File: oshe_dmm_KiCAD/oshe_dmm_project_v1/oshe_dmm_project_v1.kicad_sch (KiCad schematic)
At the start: 70 parts, among them J1 FTDI Basic, J2 USB_C_Receptacle_PowerOnly_6P, J3 ON/OFF, SW1 SW_Push, SW2 SW_Rotary_1x4_MP, U1 ATmega328P-A, U2 INA219BxD, U3 BQ24075RGT, U4 LM317_SOT-223, U5 MCP6001-OT, U6 ADS1115IDGS, Y1 16MHz

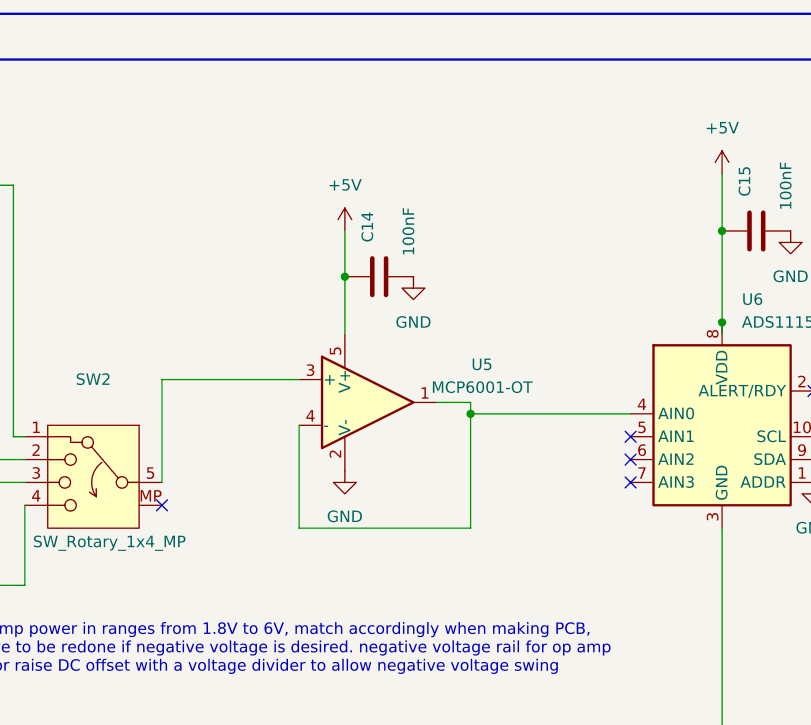
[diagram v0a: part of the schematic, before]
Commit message: updated voltage circuit.
Allows negative voltage measurement
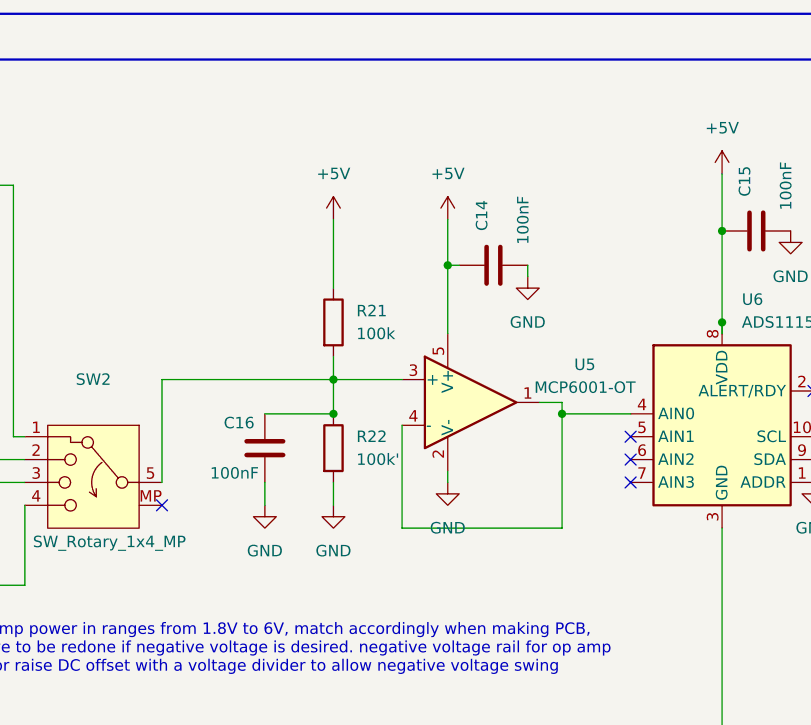
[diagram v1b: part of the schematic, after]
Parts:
- added C16: 100nF, symbol Device:C
- added R21: 100k, symbol Device:R
- added R22: 100k', symbol Device:R
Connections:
- net +5V: now also R21.1
- net GND: now also C16.2, R22.2
- net at SW2.5, U5.3 (+): now also C16.1, R21.2, R22.1
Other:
- moved on the sheet: C14, U5

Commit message: ,,k
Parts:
- added R1: 220K, Resistor_SMD:R_1206_3216Metric, symbol Device:R_US
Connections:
- net +5V: now also R1.1; no longer DS1.15 (LED(+))
- new net: DS1.15 (LED(+)), R1.2
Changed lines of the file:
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@@
 	(wire
 		(pts
+			(xy 190.5 44.45) (xy 193.04 44.45)
+		)
+		(stroke
+			(width 0)
+			(type default)
+		)
+	)
+	(wire
+		(pts
 			(xy 236.22 73.66) (xy 236.22 74.93)
 		)
@@
 	(wire
 		(pts
-			(xy 176.53 36.83) (xy 180.34 36.83)
+			(xy 176.53 36.83) (xy 190.5 36.83)
 		)
 		(stroke
@@
 	(label "R-ILIM"
 		(at 294.64 69.85 0)
-		(fields_autoplaced yes)
 		(effects
 			(font
@@
 	(label "200v"
 		(at 265.43 187.96 0)
-		(fields_autoplaced yes)
 		(effects
 			(font
@@
 	(label "200mv"
 		(at 265.43 143.51 0)
-		(fields_autoplaced yes)
 		(effects
 			(font
@@
 	(label "20v"
 		(at 262.89 176.53 0)
-		(fields_autoplaced yes)
 		(effects
 			(font
@@
 	(label "R-ISET"
 		(at 303.53 69.85 0)
-		(fields_autoplaced yes)
 		(effects
 			(font
@@
 	(label "2v"
 		(at 264.16 158.75 0)
-		(fields_autoplaced yes)
 		(effects
 			(font
@@
 	(global_label "+5V"
 		(shape input)
-		(at 180.34 36.83 0)
+		(at 193.04 44.45 0)
 		(fields_autoplaced yes)
 		(effects
@@
 		)
 		(property "Intersheetrefs" "${INTERSHEET_REFS}"
-			(at 187.1957 36.83 0)
+			(at 199.8957 44.45 0)
 			(effects
 				(font
@@
 					(unit 1)
 				)
+			)
+		)
+	)
+	(symbol
+		(lib_name "R_US_1")
+		(lib_id "Device:R_US")
+		(at 190.5 40.64 180)
+		(unit 1)
+		(exclude_from_sim no)
+		(in_bom yes)
+		(on_board yes)
+		(dnp no)
+		(fields_autoplaced yes)
+		(property "Reference" "R1"
+			(at 193.04 39.3699 0)
+			(effects
+				(font
+					(size 1.27 1.27)
+				)
+				(justify right)
+			)
+		)
+		(property "Value" "220K"
+			(at 193.04 41.9099 0)
+			(effects
+				(font
+					(size 1.27 1.27)
+				)
+				(justify right)
+			)
+		)
+		(property "Footprint" "Resistor_SMD:R_1206_3216Metric"
+			(at 189.484 40.386 90)
+			(effects
+				(font
+					(size 1.27 1.27)
+				)
+				(hide yes)
+			)
+		)
+		(property "Datasheet" "~"
+			(at 190.5 40.64 0)
+			(effects
+				(font
+					(size 1.27 1.27)
+				)
+				(hide yes)
+			)
+		)
+		(property "Description" "Resistor, US symbol"
+			(at 190.5 40.64 0)
+			(effects
+				(font
+					(size 1.27 1.27)
+				)
+				(hide yes)
+			)
+		)
+		(pin "1"
+		)
+		(pin "2"
+		)
+		(instances
+			(project ""
+				(path "/24c8480a-c336-4df0-8536-7016ee8fc0ac"
+					(reference "R1")
+					(unit 1)
+				)

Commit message: More changes plus custom footprints and symbols!
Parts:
- removed SW1: SW_Push, Button_Switch_SMD:SW_Push_1P1T-MP_NO_Horizontal_Alps_SKRTLAE010, symbol Switch:SW_Push
- added F1: 5A, Fuse:Fuseholder_Clip-5x20mm_Keystone_3512P_Inline_P23.62x7.27mm_D1.02x2.41x1.02x1.57mm_Horizontal, symbol Device:Fuse
- added SW1: PTS526 SK15 SMTR2 LFS, DMM_Footprint_Library:SMT_FS, symbol DMM_Symbol_Library:PTS526_SK15_SMTR2_LFS
- F2: renamed from F1; value Fuse -> 500mA
- renumbered C16 to C10, C14 to C11, C10 to C12, C11 to C13, C15 to C14, C12 to C15, C13 to C16, R2 to R1, R15 to R10, R16 to R11, R17 to R12, R18 to R13, R9 to R14, R10 to R15, R11 to R16, R21 to R17, R22 to R18, R12 to R19, R1 to R2, R14 to R20, R13 to R21, R19 to R22, R20 to R23, R4 to R3, R3 to R4, R1 to R8, R8 to R9, RV2 to RV1, RV1 to RV2, U5 to U4, U4 to U5
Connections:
- net Current Positive: now also F1.1; no longer R1.1, U2.8 (IN+)
- net GND: now also SW1.3, SW1.4
- net at C5.1, R7.1, U1.29 (~{RESET}/PC6): now also SW1.1, SW1.2
- new net: F1.2, R1.1, U2.8 (IN+)
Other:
- note added: "Switching System"
- note added: "Voltage Input Protection"
- note removed: "Input Protection"
- moved on the sheet: C2, C4, COMin1, D1, DS1, F2, R1, R2, R3, R4, R5, R8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

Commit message: Friday Library Meeting
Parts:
- removed C10, C11: 100nF, symbol Device:C
- removed C4: 0.15 μf, oshe:CKG57K, symbol Device:C
- removed COMin1, Vin1: ~, symbol oshe:Input
- removed D1: SMAJ200CA, Diode_SMD:D_SMA, symbol Diode:SMAJ200CA
- removed R12: 9k, symbol Device:R
- removed R17: 100k, symbol Device:R
- removed R18: 100k', symbol Device:R
- removed RV2: Varistor, symbol Device:Varistor
- removed SW2: SW_Rotary_1x4_MP, symbol Switch:SW_Rotary_1x4_MP
- removed TP1: V-, symbol Connector:TestPoint_Probe
- removed TP2: V+, symbol Connector:TestPoint_Probe
- removed U4: MCP6001-OT, Package_TO_SOT_SMD:SOT-23-5, symbol Amplifier_Operational:MCP6001-OT
- removed Vout+1, Vout-1: ~, symbol oshe:Node
- added D5: D_TVS, symbol Device:D_TVS
- added D6: SMAJ200CA, Diode_SMD:D_SMA, symbol Diode:SMAJ200CA
- added J4: Voltage, CONN_575-8_KEY, symbol DMM_Symbol_Library:575-8
- added J5: GND, CONN_575-8_KEY, symbol DMM_Symbol_Library:575-8
- added J6: Current, CONN_575-8_KEY, symbol DMM_Symbol_Library:575-8
- added R12: 1k, Resistor_SMD:R_1206_3216Metric_Pad1.30x1.75mm_HandSolder, symbol Device:R_US
- C14: footprint (none) -> Capacitor_SMD:C_1206_3216Metric_Pad1.33x1.80mm_HandSolder
- R10, R11, R22, R23: footprint (none) -> Resistor_SMD:R_1206_3216Metric_Pad1.30x1.75mm_HandSolder
- R13: value 1k -> 10k; footprint (none) -> Resistor_SMD:R_1206_3216Metric_Pad1.30x1.75mm_HandSolder
- R2: value R_US -> 1k
- R3: value 10k -> 1k
- R8: footprint Resistor_SMD:R_1206_3216Metric -> Resistor_SMD:R_1206_3216Metric_Pad1.30x1.75mm_HandSolder
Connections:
- net 200mv is gone; now on net 2V_Rang: R10.1
- net 20v is gone; now on net 200V_Rang: R11.2
- net Current Negative is gone; now on net Input_Negative: R1.2, U2.7 (IN-)
- net A0: now also R2.1, R3.1, R12.1
- net GND: no longer R13.2
- net Voltage_Input: now reaches F2.1
- net Voltage_Input: now also J4.1
- net 2V_Rang: now reaches F2.2
- net 2V_Rang: now also D6.2 (A2); no longer R2.1
- net at R2.2: no longer R3.1
- net V_ADC_Input: now reaches U6.4 (AIN0)
- net V_ADC_Input: now also D5.2 (A2)
- net Input_Negative: now reaches U6.5 (AIN1)
- net Input_Negative: now also R13.2, D5.1 (A1), D6.1 (A1), J5.1
- net 200v renamed 200V_Rang
- net 2v renamed 20V_Rang
- net Current Positive renamed Current_Input
- net Current_Input: now also J6.1
- no-connect marks 12 -> 10
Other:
- note added: "Finish switching mechanism (modes going to right spot, range indications) pick out components (custom footprints?) finalize BoM"
- note removed: "Op amp power in ranges from 1.8V to 6V, match accordingly when making PCB, will have to be redone if negative voltage is desired. negative voltage rail for op amp or raise DC offset with a voltage divider to allow negative voltage swing"
- note removed: "Voltage Input Protection"
- moved on the sheet: C14, F1, R10, R11, R13, R22, R23, U6

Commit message: Made some updates
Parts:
- removed C14: 100nF, Capacitor_SMD:C_1206_3216Metric_Pad1.33x1.80mm_HandSolder, symbol Device:C
- added C11: 0.1uF, Capacitor_SMD:C_1206_3216Metric_Pad1.33x1.80mm_HandSolder, symbol Device:C
- added J10, J9: Voltage Range 2, Connector_PinHeader_2.54mm:PinHeader_1x02_P2.54mm_Vertical, symbol Connector_Generic:Conn_01x02
- added J11, J12: Voltage Range 3, Connector_PinHeader_2.54mm:PinHeader_1x02_P2.54mm_Vertical, symbol Connector_Generic:Conn_01x02
- added J13: Current, Connector_PinHeader_2.54mm:PinHeader_1x02_P2.54mm_Vertical, symbol Connector_Generic:Conn_01x02
- added J14, J15: Resistance, Connector_PinHeader_2.54mm:PinHeader_1x02_P2.54mm_Vertical, symbol Connector_Generic:Conn_01x02
- added J7, J8: Voltage Range 1, Connector_PinHeader_2.54mm:PinHeader_1x02_P2.54mm_Vertical, symbol Connector_Generic:Conn_01x02
- added R10, R9: 1k, Resistor_SMD:R_1206_3216Metric_Pad1.30x1.75mm_HandSolder, symbol Device:R_US
- J2: renamed from J4; footprint CONN_575-8_KEY -> DMM_Footprint_Library:CONN_575-8_KEY
- J3: renamed from J5; footprint CONN_575-8_KEY -> DMM_Footprint_Library:CONN_575-8_KEY
- J4: renamed from J6; footprint CONN_575-8_KEY -> DMM_Footprint_Library:CONN_575-8_KEY
- R14: renamed from R10; symbol Device:R -> Device:R_US
- R15: renamed from R11; symbol Device:R -> Device:R_US
- R16: renamed from R13; symbol Device:R -> Device:R_US
- R22, R23: symbol Device:R -> Device:R_US
- renumbered C13 to C10, C15 to C12, C16 to C13, C3 to C2, C2 to C3, C5 to C4, C6 to C5, C7 to C6, C8 to C7, C9 to C8, C12 to C9, D2 to D1, D6 to D2, D5 to D3, D3 to D4, D4 to D5, J2 to J5, J3 to J6, R8 to R11, R9 to R12, R14 to R13, R15 to R17, R16 to R18, R4 to R2, R2 to R3, R3 to R4, R12 to R5, R5 to R7, R7 to R8, U5 to U4, U6 to U5
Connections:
- net +5V: now also C11.2, J10.1 (Pin_1), J12.1 (Pin_1), J13.1 (Pin_1), J15.1 (Pin_1), J8.1 (Pin_1)
- net 200V_Rang: now also J11.1 (Pin_1)
- net 20V_Rang: now also J9.1 (Pin_1)
- net 2V_Rang: now also D2.1 (A1), J7.1 (Pin_1); no longer D2.2 (A2)
- net A0: no longer R3.1, R4.1, R5.1
- net A3: now also R3.1, R4.1, R5.1, R10.1, R9.1
- net GND: now also C11.1
- net Input_Negative: now also D2.2 (A2); no longer D2.1 (A1)
- net V_ADC_Input: now also J11.2 (Pin_2), J7.2 (Pin_2), J9.2 (Pin_2)
- net Voltage_Input: now also J14.1 (Pin_1)
- net at R4.2: now also J10.2 (Pin_2)
- net at R5.2: now also J12.2 (Pin_2)
- net at R3.2: now also J8.2 (Pin_2)
- new net: J13.2 (Pin_2), R9.2
- new net: J15.2 (Pin_2), R10.2
- new net R_ADC_Input: J14.2 (Pin_2)
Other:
- note added: "Input Jacks"
- moved on the sheet: D2, D3, F2, J2, J3, J4, R2, R3, R4, R5, R7, U5

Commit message: Trying to fit everything on the board
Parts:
- D2: renamed from D3; footprint (none) -> Diode_SMD:D_0805_2012Metric_Pad1.15x1.40mm_HandSolder
- F1: renamed from F2; footprint Fuse:Fuseholder_Clip-5x20mm_Keystone_3512P_Inline_P23.62x7.27mm_D1.02x2.41x1.02x1.57mm_Horizontal -> DMM_Footprint_Library:FUSE_4628
- F2: renamed from F1; footprint Fuse:Fuseholder_Clip-5x20mm_Keystone_3512P_Inline_P23.62x7.27mm_D1.02x2.41x1.02x1.57mm_Horizontal -> DMM_Footprint_Library:FUSE_4628
- renumbered C9 to C10, C10 to C11, C11 to C7, C7 to C8, C8 to C9, D2 to D1, D1 to D3, R23 to R10, R17 to R14, R18 to R15, R3 to R16, R4 to R17, R5 to R18, R14 to R2, R9 to R22, R10 to R23, R15 to R3, R16 to R4, R2 to R5, R7 to R6, R6 to R7, R22 to R9, U5 to U3, U3 to U4, U4 to U5
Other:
- moved on the sheet: C7, D1, D2, F1, J10, J11, J12, J13, J14, J15, J7, J8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

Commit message: PCB is almost done!
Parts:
- removed J14, J15: Resistance, Connector_PinHeader_2.54mm:PinHeader_1x02_P2.54mm_Vertical, symbol Connector_Generic:Conn_01x02
- removed R23: 1k, Resistor_SMD:R_1206_3216Metric_Pad1.30x1.75mm_HandSolder, symbol Device:R_US
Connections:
- net MISO/D12: now also DS1.4 (RS); no longer DS1.6 (E)
- net MOSI/D11: now also DS1.6 (E); no longer DS1.4 (RS)

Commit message: Final V1 PCB?!?!?!?
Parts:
- added TP1, TP2: SDA, TestPoint:TestPoint_Keystone_5019_Minature, symbol Connector:TestPoint
- D2: value D_TVS -> VS4V8BU1ART7R
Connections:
- net SCL: now also TP2.1
- net SDA: now also TP1.1
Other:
- note added: "alert ready pin is used for interrupt based designs?"
- note removed: "Finish switching mechanism (modes going to right spot, range indications) pick out components (custom footprints?) finalize BoM"
- note removed: "a 10k pullup resistor is needed for SDA and SCL, probably already in schematic at microcontroller side. check for those at design meet."
- note removed: "alert ready pin is used for interrupt based designs. ask questions at meeting."
- moved on the sheet: C3, F2, J10, J11, J12, J13, J7, J8, J9, R1, R16, R17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
